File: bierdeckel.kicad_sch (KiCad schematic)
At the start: 33 parts, among them SW1 Adress Coding, U1 TPS61201DRC, U2 ESP32-C3-WROOM-02

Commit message: bla
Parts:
- removed C1, C2: 330mF, bier:super_cap, symbol bier:C_super
- removed C3: 0.1uF, Capacitor_SMD:C_0805_2012Metric, symbol Device:C
- removed C4, C5: 10uF, Capacitor_SMD:C_0805_2012Metric, symbol Device:C
- removed D1: WS2812B 2020 Flipped, bier:ws2812B_2020_flipped, symbol bier:WS2812B_2020_flipped
- removed D2, D3, D4, D5, D6, D7, D8, D9: WS2812B, LED_SMD:LED_WS2812B-2020_PLCC4_2.0x2.0mm, symbol LED:WS2812B
- removed L1: 2.2µH, Resistor_SMD:R_0805_2012Metric, symbol Device:L
- removed R1, R2: R, Resistor_SMD:R_0805_2012Metric, symbol Device:R
- removed R4: 10k, Resistor_SMD:R_0805_2012Metric, symbol Device:R
- removed TP1, TP2: TestPoint, TestPoint:TestPoint_Pad_D3.0mm, symbol Connector:TestPoint
- removed U1: TPS61201DRC, Package_SON:Texas_S-PVSON-N10_ThermalVias, symbol Regulator_Switching:TPS61201DRC
- added B1, B10, B2, B3, B4, B5, B6, B7, B8: 0R, Resistor_SMD:R_1206_3216Metric, symbol Device:R
- added J7: S70-332002045R, bier:pogo_receptor, symbol bier:Pogo_receptor
- added SW2: PTS526 SK15 SMTR2 LFS, Button_Switch_SMD:SW_Push_1P1T_XKB_TS-1187A, symbol Switch:SW_Push
- added U3: ATtiny84A-SS, Package_SO:SOIC-14_3.9x8.7mm_P1.27mm, symbol MCU_Microchip_ATtiny:ATtiny84A-SS
- C6: mpn (none) -> CL21B105KAFNNNG
- C7: mpn (none) -> CL21A106KPFNNNF
- C8: mpn (none) -> KGM21NR71H104KT
- J1, J2, J3, J4, J5, J6: value ~ -> S70-332002045R; mpn (none) -> S70-332002045R; now left out of the parts list
- R3: mpn (none) -> CR0805-FX-1002ELF
- SW1: value Adress Coding -> Address Coding; mpn (none) -> 219-5LPSTR
- U2: mpn (none) -> ESP32-C3-WROOM-02-N4
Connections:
- net +3.3V: now also B4.1, B4.2, U3.1 (VCC)
- net AD0: now also SW1.4, U3.2 (XTAL1/PB0); no longer SW1.3
- net AD1: now also SW1.5, U3.3 (XTAL2/PB1); no longer SW1.4
- net AD2: now also U3.13 (AREF/PA0)
- net AD3: now also U3.11 (PA2)
- net GND: now also SW1.6, B1.1, B1.2, B10.1, B10.2, B2.1, B2.2, B3.1, B3.2, B6.1, B6.2, B7.1, B7.2, B8.1, B8.2, SW2.1, U3.14 (GND); no longer SW1.8
- net LED_DATA: now also U3.12 (PA1)
- net Vpress: now also U3.10 (PA3)
- net Vreg_in: now also SW1.8; no longer SW1.5
- net RST: now reaches C6.1, R3.2, U2.2 (EN/CHIP_PU)
- net RST: now also J4.1 (pogo_receptor), SW2.2, U3.4 (~{RESET}/PB3)
- net TCK renamed MOSI
- net MOSI: now also U3.7 (PA6)
- net TDI renamed SCK
- net SCK: now also J7.1 (pogo_receptor), U3.9 (PA4); no longer J4.1 (pogo_receptor)
- net TMS renamed MISO
- net MISO: now also U3.8 (PA5)
- net Vcap renamed Vcharge
- net Vcharge: no longer SW1.6
- new net Vbat: B5.1, B5.2, SW1.3
- no-connect marks 0 -> 7
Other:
- added sheet LEDs (leds.kicad_sch)
- added sheet PSU (power.kicad_sch)
- added sheet Pressure Gauge (pressure.kicad_sch)
- note added: "Address Coding"
- note added: "Bridges"
- note added: "Power Supply"
- note removed: "LEDs"
- note removed: "Reset button?"
- note removed: "Voltage Supply"
- note removed: "Vpress = Vcc*R1/(Rs+R1) => F = Rs = ((Vcc*R1)-Vpress*R1)/Vpress"
- moved on the sheet: C6, C7, C8, R3, SW1, U2

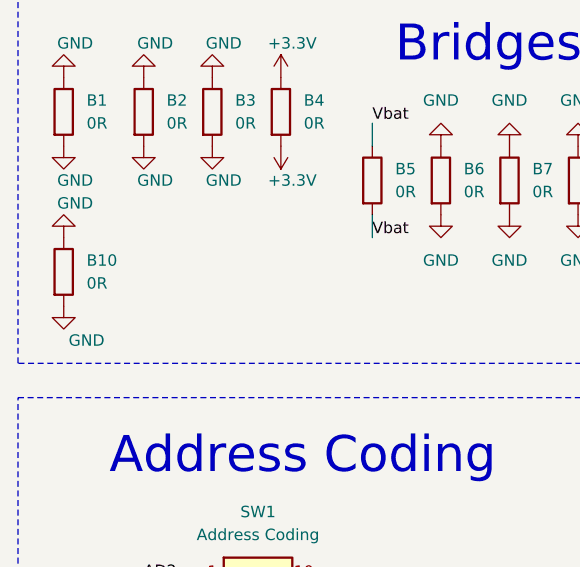
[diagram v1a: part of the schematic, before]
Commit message: Implement Simon's layout suggestions
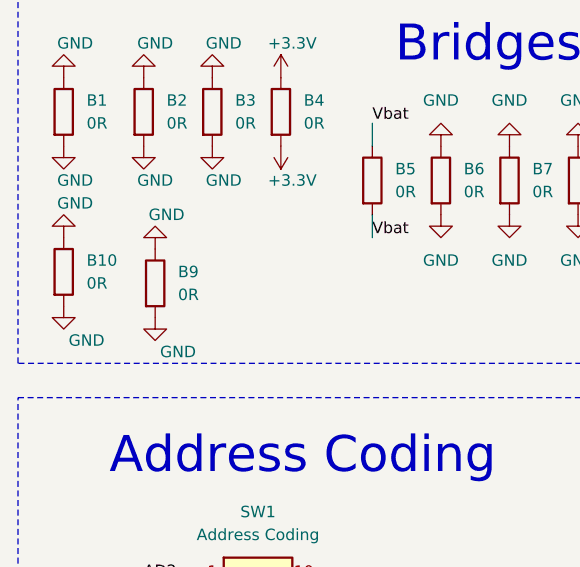
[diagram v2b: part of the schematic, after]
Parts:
- added B9: 0R, Resistor_SMD:R_1206_3216Metric, symbol Device:R
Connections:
- net GND: now also B9.1, B9.2
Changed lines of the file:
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@@
+    )
+  )
+  (symbol (lib_id "power:GND") (at 30.48 97.79 0) (unit 1)
+    (in_bom yes) (on_board yes) (dnp no)
+    (property "Reference" "#PWR062" (at 30.48 104.14 0)
+      (effects (font (size 1.27 1.27)) hide)
+    )
+    (property "Value" "GND" (at 33.02 101.6 0)
+      (effects (font (size 1.27 1.27)))
+    )
+    (property "Footprint" "" (at 30.48 97.79 0)
+      (effects (font (size 1.27 1.27)) hide)
+    )
+    (property "Datasheet" "" (at 30.48 97.79 0)
+      (effects (font (size 1.27 1.27)) hide)
+    )
+    (pin "1")
+    (instances
+      (project "bierdeckel"
+        (path "/a4ffe097-37ef-4e19-a91a-ae57f4a5aad1"
+          (reference "#PWR062") (unit 1)
+        )
+      )
     )
   )
@@
     )
   )
+  (symbol (lib_id "Device:R") (at 30.48 93.98 0) (unit 1)
+    (in_bom yes) (on_board yes) (dnp no)
+    (property "Reference" "B9" (at 33.02 92.71 0)
+      (effects (font (size 1.27 1.27)) (justify left))
+    )
+    (property "Value" "0R" (at 33.02 95.25 0)
+      (effects (font (size 1.27 1.27)) (justify left))
+    )
+    (property "Footprint" "Resistor_SMD:R_1206_3216Metric" (at 28.702 93.98 90)
+      (effects (font (size 1.27 1.27)) hide)
+    )
+    (property "Datasheet" "~" (at 30.48 93.98 0)
+      (effects (font (size 1.27 1.27)) hide)
+    )
+    (property "mpn" "CR1206-J/-000ELF" (at 30.48 93.98 0)
+      (effects (font (size 1.27 1.27)) hide)
+    )
+    (pin "1")
+    (pin "2")
+    (instances
+      (project "bierdeckel"
+        (path "/a4ffe097-37ef-4e19-a91a-ae57f4a5aad1"
+          (reference "B9") (unit 1)
+        )
+      )
+    )
+  )
   (symbol (lib_id "Device:R") (at 69.85 82.55 0) (unit 1)
     (in_bom yes) (on_board yes) (dnp no) (fields_autoplaced)
@@
       (effects (font (size 1.27 1.27)) hide)
     )
-    (property "Datasheet" "https://www.digikey.at/en/products/detail/c-k/PTS526-SK15-SMTR2-LFS/10056626" (at 151.13 64.77 0)
+    (property "Datasheet" "~" (at 151.13 64.77 0)
       (effects (font (size 1.27 1.27)) hide)
     )
@@
         )
       )
+    )
+  )
+  (symbol (lib_id "power:GND") (at 30.48 90.17 180) (unit 1)
+    (in_bom yes) (on_board yes) (dnp no)
+    (property "Reference" "#PWR061" (at 30.48 83.82 0)
+      (effects (font (size 1.27 1.27)) hide)
+    )
+    (property "Value" "GND" (at 31.75 86.36 0)
+      (effects (font (size 1.27 1.27)))
+    )
+    (property "Footprint" "" (at 30.48 90.17 0)
+      (effects (font (size 1.27 1.27)) hide)
+    )
+    (property "Datasheet" "" (at 30.48 90.17 0)
+      (effects (font (size 1.27 1.27)) hide)
+    )
+    (pin "1")
+    (instances
+      (project "bierdeckel"
+        (path "/a4ffe097-37ef-4e19-a91a-ae57f4a5aad1"
+          (reference "#PWR061") (unit 1)
+        )
+      )

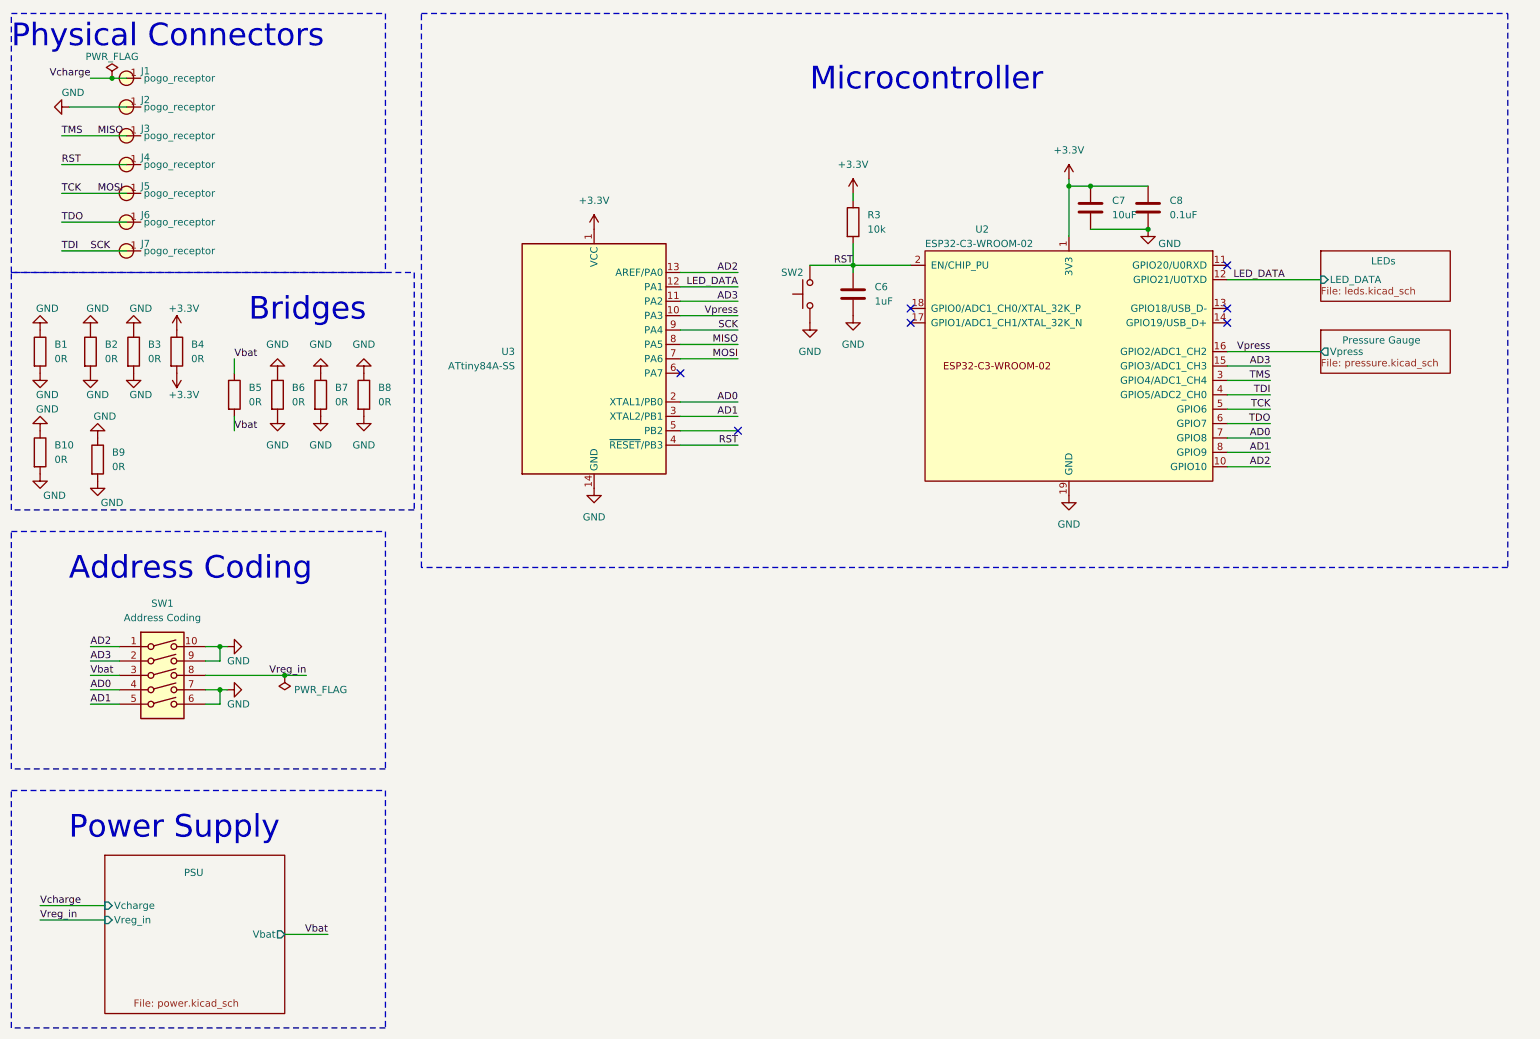
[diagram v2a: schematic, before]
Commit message: remove ATTiny; fix LED footprints; start cleanup
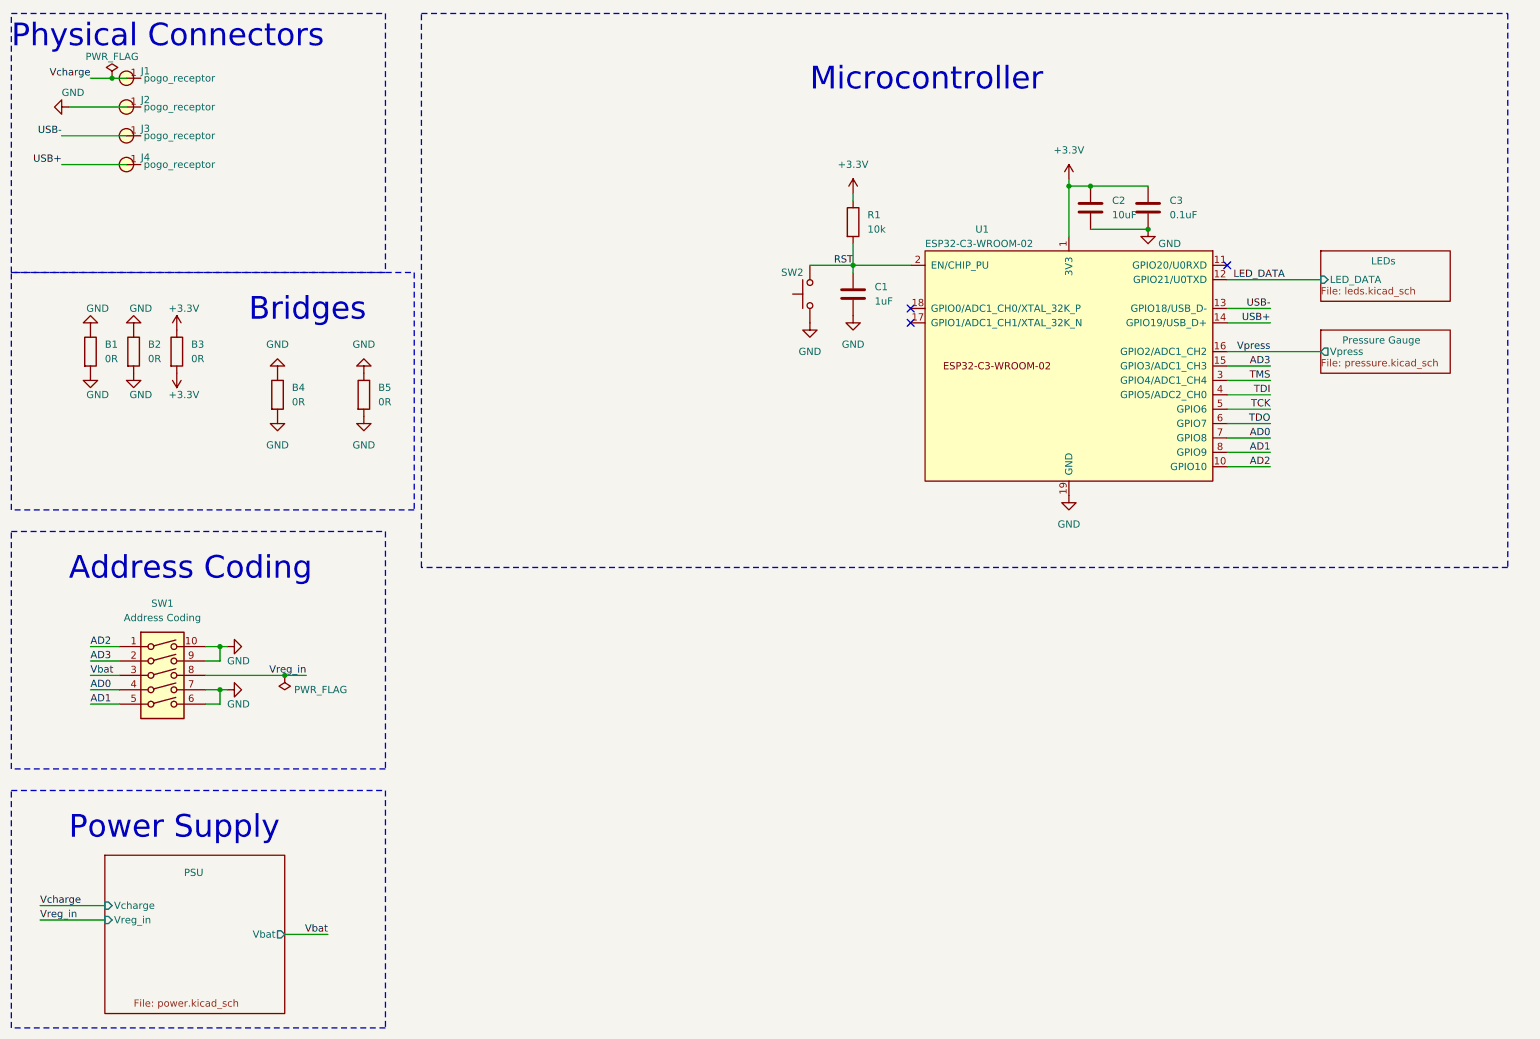
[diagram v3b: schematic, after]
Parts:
- removed B1, B10, B5, B7, B9: 0R, Resistor_SMD:R_1206_3216Metric, symbol Device:R
- removed J5, J6, J7: S70-332002045R, bier:pogo_receptor, symbol bier:Pogo_receptor
- removed U3: ATtiny84A-SS, Package_SO:SOIC-14_3.9x8.7mm_P1.27mm, symbol MCU_Microchip_ATtiny:ATtiny84A-SS
- renumbered B2 to B1, B3 to B2, B4 to B3, B6 to B4, B8 to B5, C6 to C1, C7 to C2, C8 to C3, R3 to R1, U2 to U1
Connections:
- net RST: no longer J4.1 (pogo_receptor)
- net USB-: now reaches U1.13 (GPIO18/USB_D-)
- net USB-: now also J3.1 (pogo_receptor)
- net USB+: now reaches U1.14 (GPIO19/USB_D+)
- net USB+: now also J4.1 (pogo_receptor)
- net MISO renamed TMS
- net TMS: no longer J3.1 (pogo_receptor)
- net MOSI renamed TCK
- net SCK renamed TDI
- no-connect marks 7 -> 3

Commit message: improve layout further
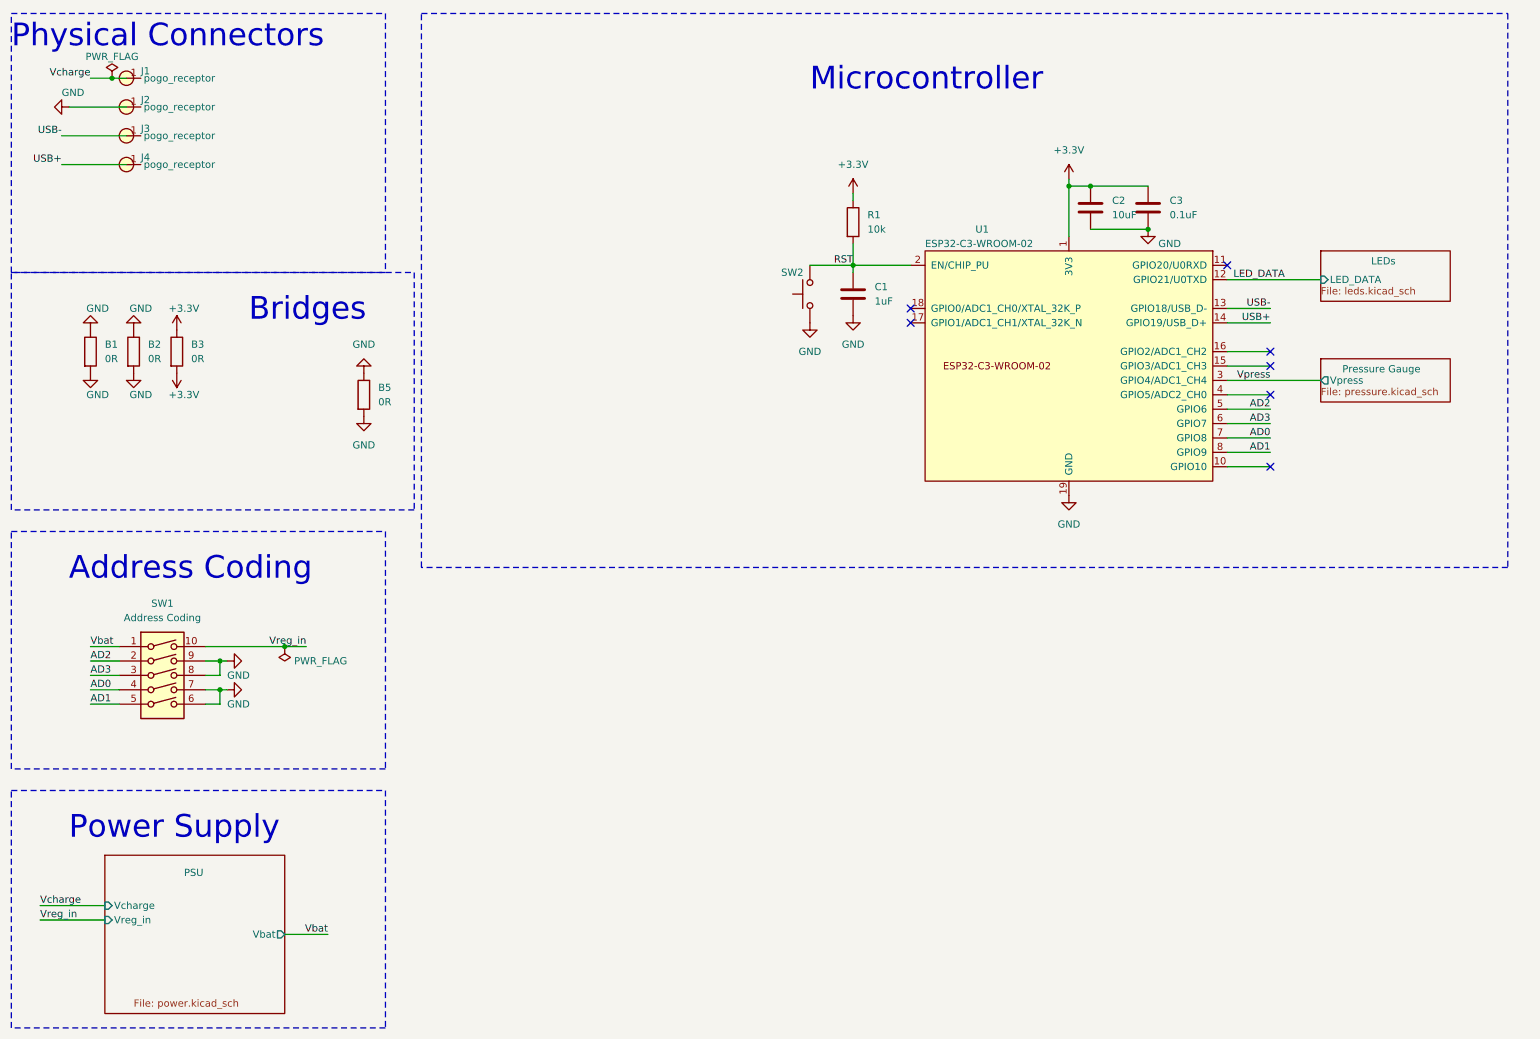
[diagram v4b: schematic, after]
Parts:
- removed B4: 0R, Resistor_SMD:R_1206_3216Metric, symbol Device:R
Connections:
- net TCK is gone; now on net AD2: U1.5 (GPIO6)
- net TDO is gone; now on net AD3: U1.6 (GPIO7)
- net TMS is gone; now on net Vpress: U1.3 (GPIO4/ADC1_CH4)
- net AD2: now also SW1.2; no longer SW1.1, U1.10 (GPIO10)
- net AD3: now also SW1.3; no longer SW1.2, U1.15 (GPIO3/ADC1_CH3)
- net GND: now also SW1.8; no longer SW1.10
- net Vbat: now also SW1.1; no longer SW1.3
- net Vpress: no longer U1.16 (GPIO2/ADC1_CH2)
- net Vreg_in: now also SW1.10; no longer SW1.8
- net TDI: no longer names the net of U1.4 (GPIO5/ADC2_CH0)
- no-connect marks 3 -> 7

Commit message: fix some layout issues
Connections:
- net AD1: no longer U1.8 (GPIO9)
- net LED_DATA: now also U1.10 (GPIO10); no longer U1.12 (GPIO21/U0TXD)
- new net ~{BOOTLOADER}: U1.8 (GPIO9)
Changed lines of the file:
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@@
 	)
 	(no_connect
-		(at 237.49 74.93)
+		(at 229.87 62.23)
 	)
 	(no_connect
-		(at 237.49 95.25)
+		(at 229.87 74.93)
 	)
 	(no_connect
@@
 	(wire
 		(pts
+			(xy 229.87 90.17) (xy 237.49 90.17)
+		)
+		(stroke
+			(width 0)
+			(type default)
+		)
+	)
+	(wire
+		(pts
+			(xy 229.87 95.25) (xy 246.38 95.25)
+		)
+		(stroke
+			(width 0)
+			(type default)
+		)
+	)
+	(wire
+		(pts
 			(xy 52.07 134.62) (xy 49.53 134.62)
 		)
@@
 	(wire
 		(pts
-			(xy 237.49 92.71) (xy 229.87 92.71)
+			(xy 243.84 92.71) (xy 229.87 92.71)
 		)
 		(stroke
@@
 	(wire
 		(pts
-			(xy 237.49 90.17) (xy 229.87 90.17)
-		)
-		(stroke
-			(width 0)
-			(type default)
-		)
-	)
-	(wire
-		(pts
-			(xy 229.87 62.23) (xy 246.38 62.23)
-		)
-		(stroke
-			(width 0)
-			(type default)
-		)
-	)
-	(wire
-		(pts
 			(xy 163.83 46.99) (xy 163.83 48.26)
 		)
@@
 	(wire
 		(pts
-			(xy 237.49 74.93) (xy 229.87 74.93)
-		)
-		(stroke
-			(width 0)
-			(type default)
-		)
-	)
-	(wire
-		(pts
 			(xy 163.83 59.69) (xy 173.99 59.69)
 		)
@@
 	(wire
 		(pts
-			(xy 237.49 95.25) (xy 229.87 95.25)
-		)
-		(stroke
-			(width 0)
-			(type default)
-		)
-	)
-	(wire
-		(pts
 			(xy 49.53 132.08) (xy 52.07 132.08)
 		)
@@
 		)
 	)
-	(label "LED_DATA"
-		(at 240.03 62.23 180)
-		(fields_autoplaced yes)
-		(effects
-			(font
-				(size 1.27 1.27)
-			)
-			(justify right bottom)
-		)
-	)
 	(label "AD3"
 		(at 29.21 132.08 0)
@@
 		)
 	)
+	(label "LED_DATA"
+		(at 241.3 95.25 180)
+		(fields_autoplaced yes)
+		(effects
+			(font
+				(size 1.27 1.27)
+			)
+			(justify right bottom)
+		)
+	)
 	(label "AD0"
 		(at 237.49 90.17 180)
@@
 		)
 	)
-	(label "AD1"
-		(at 237.49 92.71 180)
+	(label "~{BOOTLOADER}"
+		(at 243.84 92.71 180)
 		(fields_autoplaced yes)
 		(effects
@@
 	)
 	(sheet
-		(at 246.38 57.15)
+		(at 246.38 91.44)
 		(size 22.86 8.89)
 		(stroke
@@
 		)
 		(property "Sheetname" "LEDs"
-			(at 255.27 59.69 0)
+			(at 255.27 93.98 0)
 			(effects
 				(font
@@
 		)
 		(property "Sheetfile" "leds.kicad_sch"
-			(at 246.38 63.5 0)
+			(at 246.38 97.79 0)
 			(effects
 				(font
@@
 		)
 		(pin "LED_DATA" input
-			(at 246.38 62.23 180)
+			(at 246.38 95.25 180)
 			(effects
 				(font
@@
 			(project "bierdeckel"
 				(path "/a4ffe097-37ef-4e19-a91a-ae57f4a5aad1"
-					(page "3")
+					(page "2")
 				)
 			)

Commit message: improve edge marker, get rid of 1 power bridge
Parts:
- removed B3: 0R, Resistor_SMD:R_1206_3216Metric, symbol Device:R
- added SW3: PTS526 SK15 SMTR2 LFS, Button_Switch_SMD:SW_Push_1P1T_XKB_TS-1187A, symbol Switch:SW_Push
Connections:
- net AD0: now also U1.6 (GPIO7); no longer U1.7 (GPIO8)
- net AD1: now also U1.7 (GPIO8)
- net AD2: now also U1.4 (GPIO5/ADC2_CH0); no longer U1.5 (GPIO6)
- net AD3: now also U1.5 (GPIO6); no longer U1.6 (GPIO7)
- net GND: now also SW3.1
- net ~{BOOTLOADER}: now also SW3.2
- no-connect marks 7 -> 6
